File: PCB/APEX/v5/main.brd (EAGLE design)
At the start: 38.1 x 38.1 mm, 5 parts

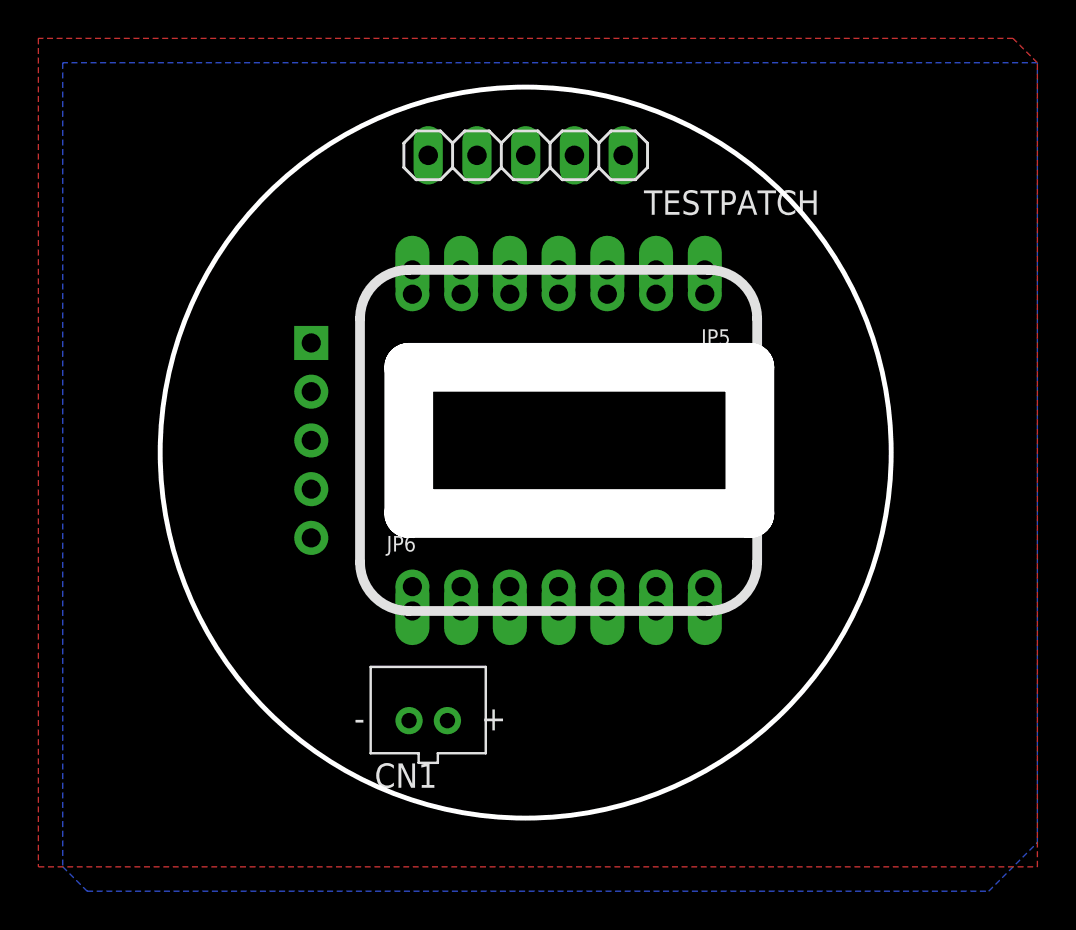
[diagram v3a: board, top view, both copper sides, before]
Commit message: reroute traces post flip
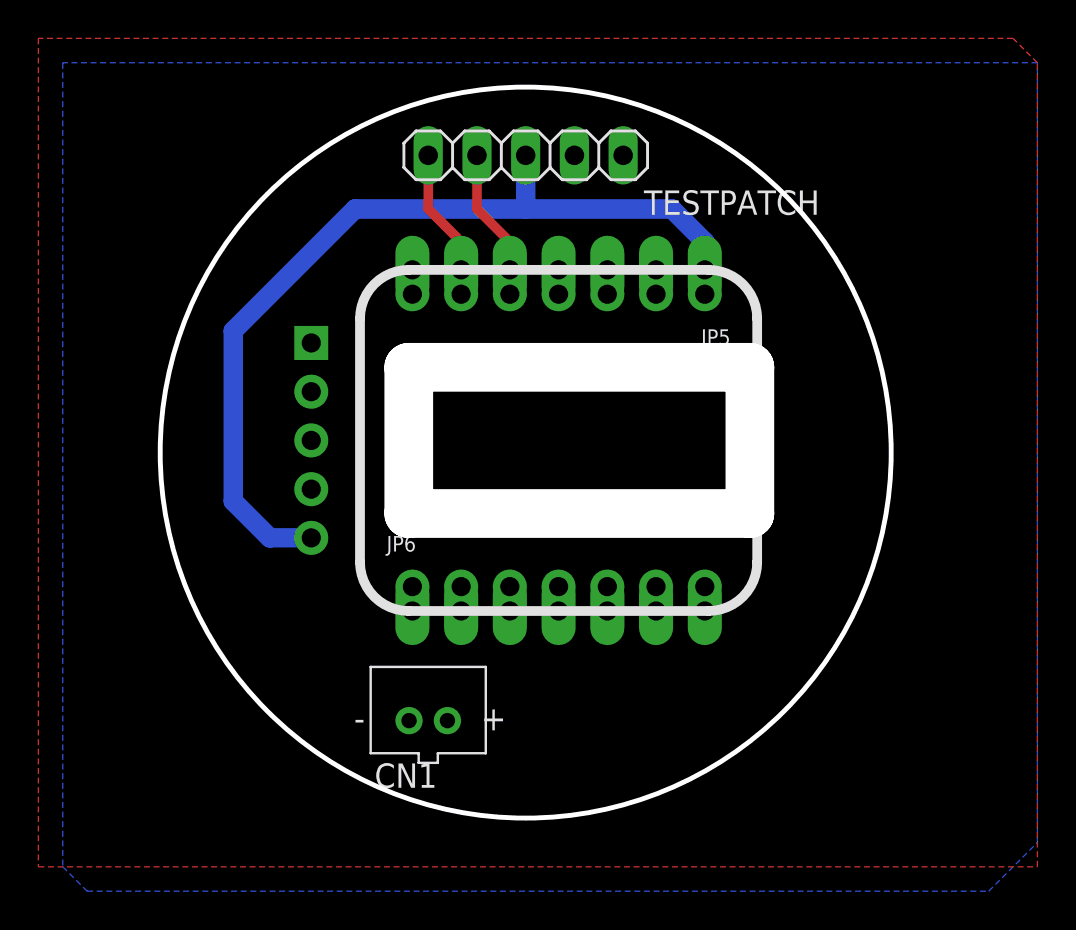
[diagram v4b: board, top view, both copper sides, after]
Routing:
- net AIN+: track 0.00 -> 45.9 mm
- net SDA: track 0.00 -> 6.68 mm
- net SCL: track 0.00 -> 6.68 mm
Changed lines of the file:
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@@
 <contactref element="JP2" pad="5"/>
 <contactref element="TESTPATCH" pad="3"/>
+<wire x1="75.3745" y1="121.285" x2="75.3745" y2="122.7455" width="1.016" layer="16"/>
+<wire x1="73.66" y1="124.46" x2="75.3745" y2="122.7455" width="1.016" layer="16"/>
+<wire x1="54.864" y1="107.315" x2="52.705" y2="107.315" width="1.016" layer="16"/>
+<wire x1="52.705" y1="107.315" x2="50.8" y2="109.22" width="1.016" layer="16"/>
+<wire x1="50.8" y1="109.22" x2="50.8" y2="118.11" width="1.016" layer="16"/>
+<wire x1="50.8" y1="118.11" x2="57.15" y2="124.46" width="1.016" layer="16"/>
+<wire x1="57.15" y1="124.46" x2="66.04" y2="124.46" width="1.016" layer="16"/>
+<wire x1="66.04" y1="124.46" x2="73.66" y2="124.46" width="1.016" layer="16"/>
+<wire x1="66.04" y1="127.254" x2="66.04" y2="124.46" width="1.016" layer="16"/>
 <wire x1="75.3745" y1="121.285" x2="75.3745" y2="120.015" width="0" layer="19" extent="1-1"/>
-<wire x1="66.04" y1="127.254" x2="75.3745" y2="120.015" width="0" layer="19" extent="1-1"/>
-<wire x1="54.864" y1="107.315" x2="66.04" y2="127.254" width="0" layer="19" extent="1-1"/>
 </signal>
 <signal name="A1">
@@
 <contactref element="JP5" pad="5C"/>
 <contactref element="TESTPATCH" pad="4"/>
+<wire x1="63.5" y1="127.254" x2="63.5" y2="124.46" width="0.508" layer="1"/>
+<wire x1="65.2145" y1="122.7455" x2="65.2145" y2="121.285" width="0.508" layer="1"/>
+<wire x1="63.5" y1="124.46" x2="65.2145" y2="122.7455" width="0.508" layer="1"/>
 <wire x1="65.2145" y1="121.285" x2="65.2145" y2="120.015" width="0" layer="19" extent="1-1"/>
-<wire x1="63.5" y1="127.254" x2="65.2145" y2="120.015" width="0" layer="19" extent="1-1"/>
 </signal>
 <signal name="SCL">
@@
 <contactref element="JP5" pad="6C"/>
 <contactref element="TESTPATCH" pad="5"/>
+<wire x1="60.96" y1="127.254" x2="60.96" y2="124.46" width="0.508" layer="1"/>
+<wire x1="62.6745" y1="122.7455" x2="62.6745" y2="121.285" width="0.508" layer="1"/>
+<wire x1="60.96" y1="124.46" x2="62.6745" y2="122.7455" width="0.508" layer="1"/>
 <wire x1="62.6745" y1="121.285" x2="62.6745" y2="120.015" width="0" layer="19" extent="1-1"/>
-<wire x1="60.96" y1="127.254" x2="62.6745" y2="120.015" width="0" layer="19" extent="1-1"/>
 </signal>
 <signal name="+3V3">

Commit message: increase clearance for stemma port
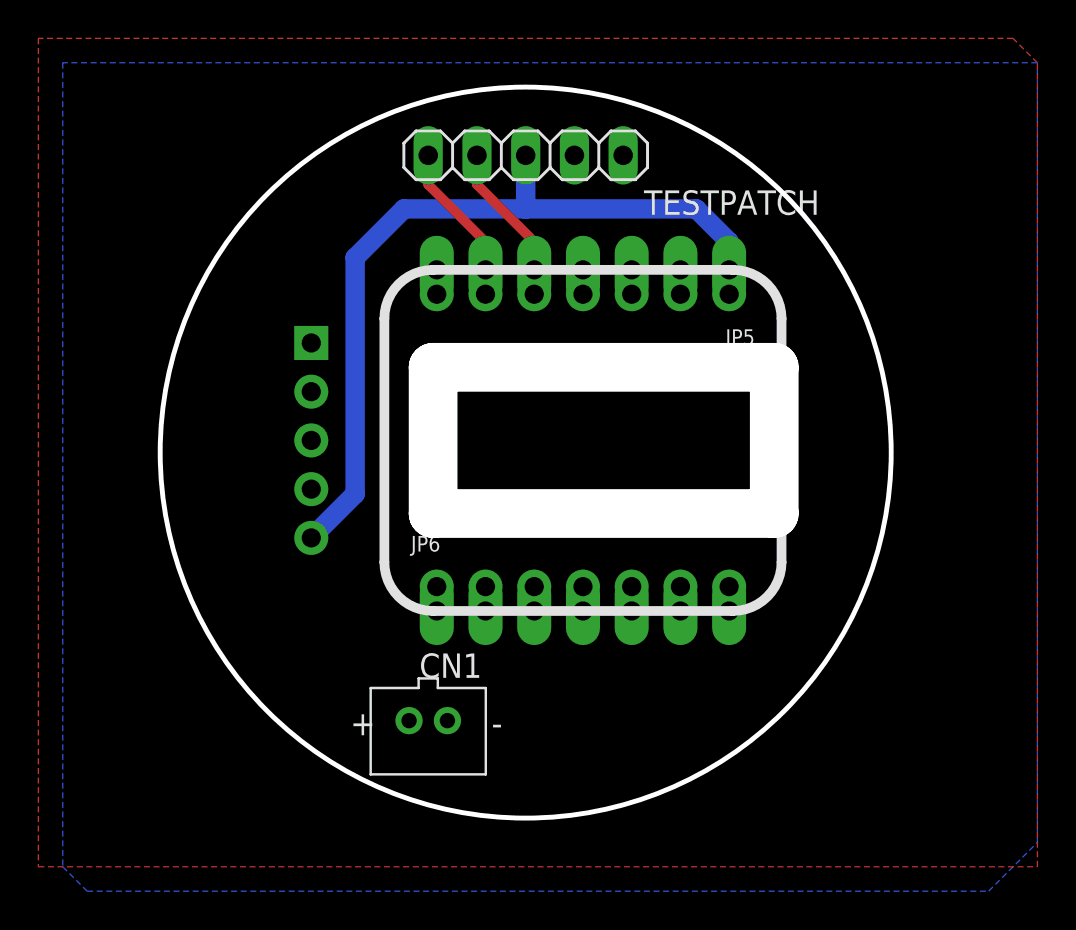
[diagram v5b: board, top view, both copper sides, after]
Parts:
- moved JP5 1.27 mm to (69.0, 120.0)
- moved JP6 1.27 mm to (69.0, 104.8)
- turned CN1 to 180 degrees
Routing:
- net AIN+: track 45.9 -> 41.1 mm
- net SDA: track 6.68 -> 7.21 mm
- net SCL: track 6.68 -> 7.21 mm
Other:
- outline, holes or cut-outs redrawn
